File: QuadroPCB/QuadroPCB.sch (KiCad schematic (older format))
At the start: 24 parts, among them IC1 AT24CS02-SSHM, P1 MPU9150, P10 AKKU, P2 stm32discovery_left, P3 stm32discovery_right, P4 rc_signal, P5 Motor3, P6 Motor4, P7 BMP180, P8 Motor1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

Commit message: blubb
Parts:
- added P11: MeisterFluglicht, Pin_Headers:Pin_Header_Straight_1x05, symbol CONN_01X05
- added Q2: Q_NMOS_GSD, Housings_SOT-23_SOT-143_TSOT-6:SOT-23_Handsoldering, symbol Q_NMOS_GSD
- added R6: 1k, Resistors_SMD:R_0805_HandSoldering, symbol R
- added SP2: SPEAKER, Buzzers_Beepers:Buzzer_12x9.5RM7.6, symbol SPEAKER
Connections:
- net +5V: now also SP1.1, SP2.1; no longer SP1.2
- net Beeper_PIN: no longer R4.1
- net GND: now also P11.5 (P5), Q2.2 (S)
- net at Q1.3 (D): now also SP1.2; no longer SP1.1
- net LEDS_SPI_SCK: now reaches P2.35 (P35)
- net LEDS_SPI_SCK: now also P11.1 (P1)
- net LEDS_SPI_SS: now reaches P2.36 (P36)
- net LEDS_SPI_SS: now also P11.2 (P2)
- net LEDS_SPI_MOSI: now reaches P2.37 (P37)
- net LEDS_SPI_MOSI: now also P11.3 (P3)
- net LEDS_SPI_MISO: now reaches P2.38 (P38)
- net LEDS_SPI_MISO: now also P11.4 (P4)
- net Beeper1_PIN: now reaches P3.3 (P3)
- net Beeper1_PIN: now also R6.1
- net Beeper2_PIN: now reaches P3.4 (P4)
- net Beeper2_PIN: now also R4.1
- new net: Q2.1 (G), R6.2
- new net: Q2.3 (D), SP2.2
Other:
- note added: "TODO:\n\nspi pins für leds\nweite pins rausführen?\n"
- note removed: "TODO:\n\nbuzzer pin\nweite pins rausführen?\n"
- moved on the sheet: P1, P4

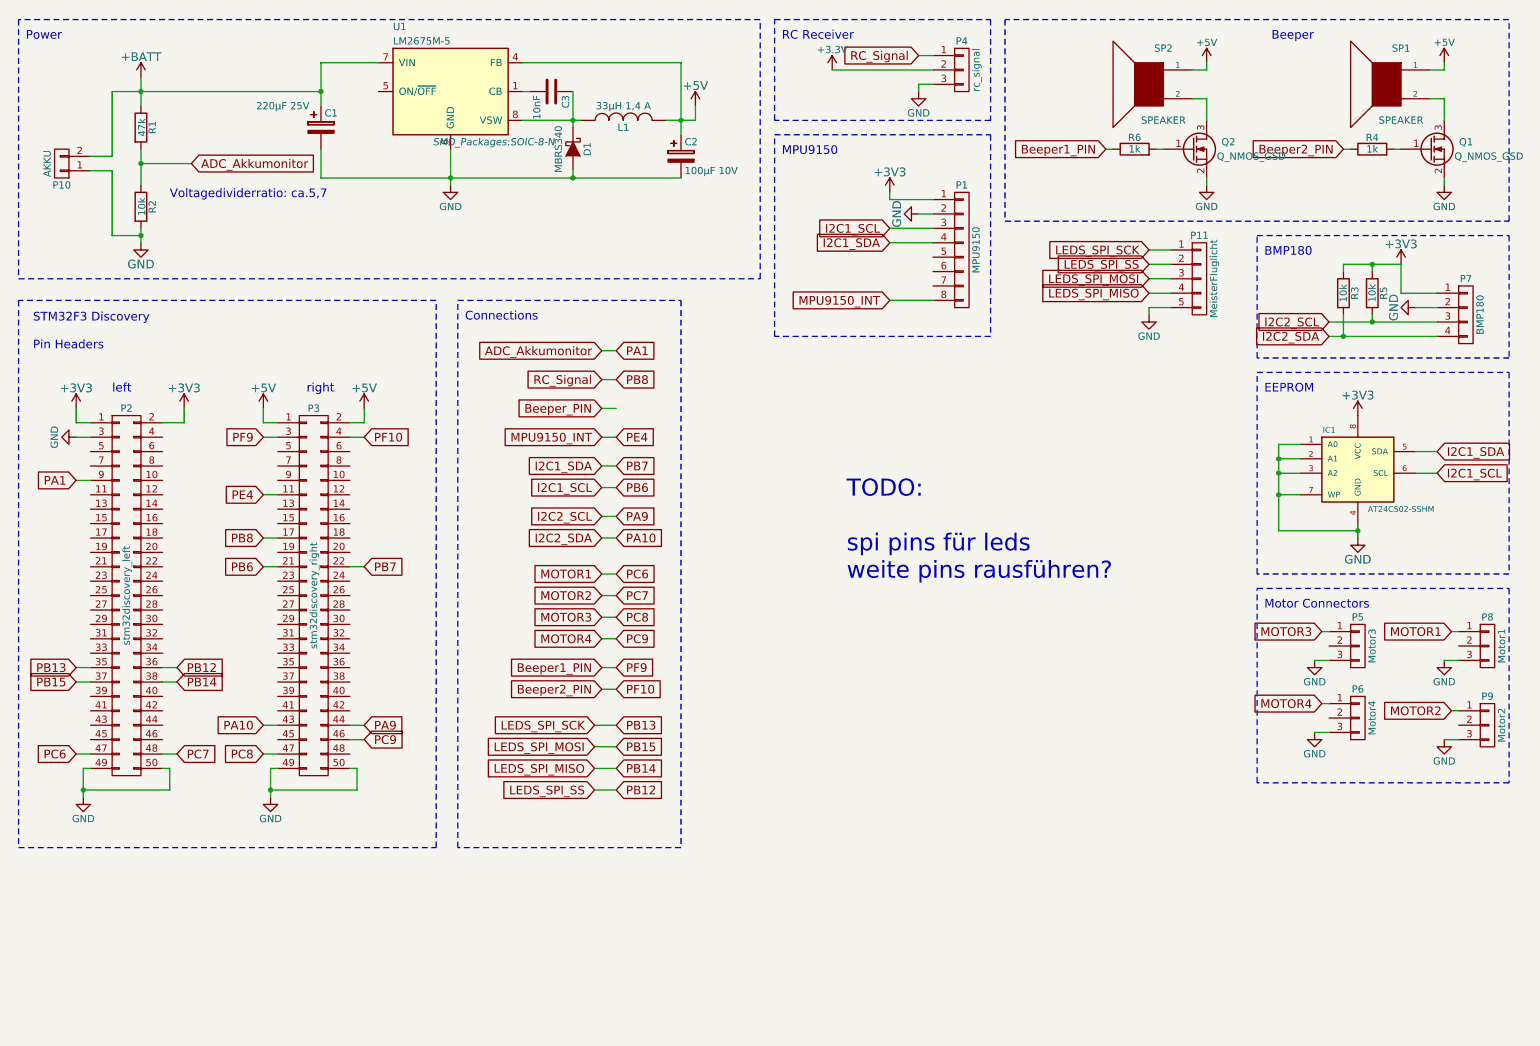
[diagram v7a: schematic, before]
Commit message: step down extern fluglicht auf die platine gepackt
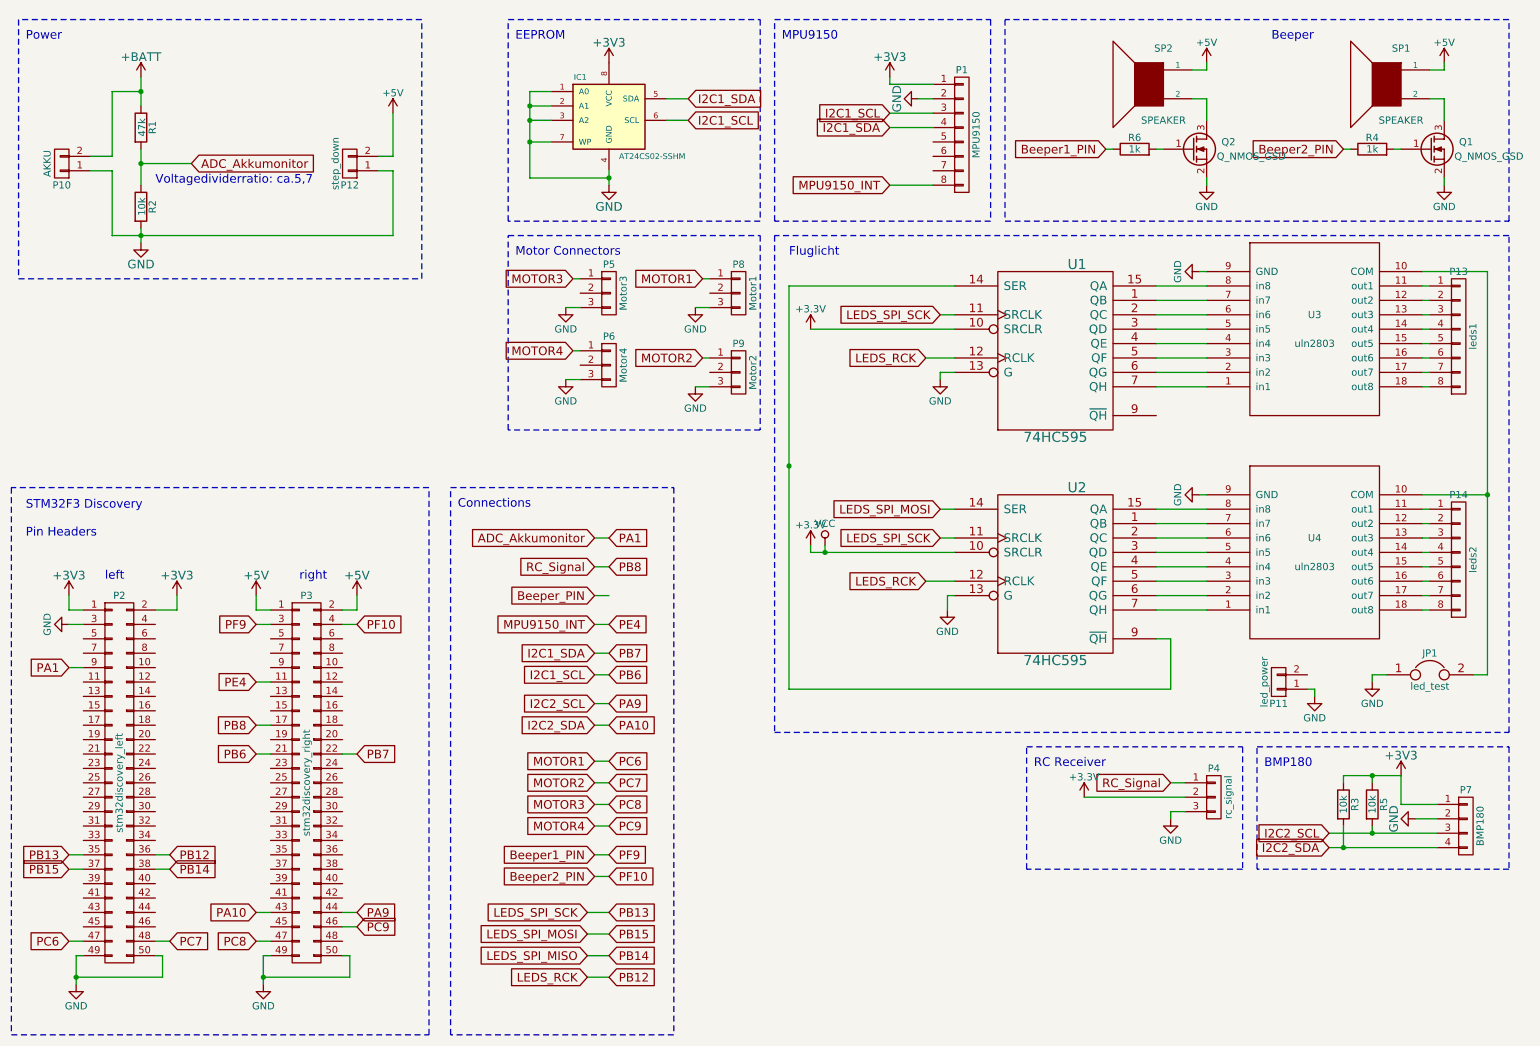
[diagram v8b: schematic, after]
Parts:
- removed C1: 220µF 25V, Capacitors_SMD:c_elec_8x10.5, symbol CP
- removed C2: 100µF 10V, Capacitors_SMD:c_elec_8x6.7, symbol CP
- removed C3: 10nF, Capacitors_SMD:C_0805_HandSoldering, symbol C
- removed D1: MBRS340, Diodes_SMD:Diode-DO-214AB_Handsoldering, symbol D_Schottky
- removed L1: 33µH 1,4 A, Choke_SMD:Choke_SMD_PISN_Handsoldering_FASTRON, symbol INDUCTOR
- removed P11: MeisterFluglicht, Pin_Headers:Pin_Header_Straight_1x05, symbol CONN_01X05
- removed U1: LM2675M-5, SMD_Packages:SOIC-8-N, symbol LM2675M-5
- added JP1: led_test, Pin_Headers:Pin_Header_Straight_1x02, symbol JUMPER
- added P11: led_power, Connect:PINHEAD1-2, symbol CONN_01X02
- added P12: step_down, Connect:PINHEAD1-2, symbol CONN_01X02
- added P13: leds1, Pin_Headers:Pin_Header_Straight_1x08, symbol CONN_01X08
- added P14: leds2, Pin_Headers:Pin_Header_Straight_1x08, symbol CONN_01X08
- added U1, U2: 74HC595, Housings_SOIC:SOIC-16_3.9x9.9mm_Pitch1.27mm, symbol 74HC595
- added U3, U4: uln2803, Housings_SOIC:SOIC-18_7.5x11.6mm_Pitch1.27mm, symbol uln2803
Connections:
- net +3V3: now also U1.10 (SRCLR), U1.16 (VCC), U2.10 (SRCLR), U2.16 (VCC)
- net +5V: now also P12.2 (P2)
- net GND: now also JP1.1, P11.1 (P1), P12.1 (P1), U1.13 (G), U1.8 (GND), U2.13 (G), U2.8 (GND), U3.9 (GND), U4.9 (GND)
- net LEDS_SPI_MOSI: now also U2.14 (SER)
- net LEDS_SPI_SCK: now also U1.11 (SRCLK), U2.11 (SRCLK)
- net LEDS_SPI_SS renamed LEDS_RCK
- net LEDS_RCK: now also U1.12 (RCLK), U2.12 (RCLK)
- new net: U2.1 (QB), U4.7 (in7)
- new net: U2.15 (QA), U4.8 (in8)
- new net: U2.2 (QC), U4.6 (in6)
- new net: U2.3 (QD), U4.5 (in5)
- new net: U2.4 (QE), U4.4 (in4)
- new net: U2.5 (QF), U4.3 (in3)
- new net: U2.6 (QG), U4.2 (in2)
- new net: U2.7 (QH), U4.1 (in1)
- new net: U1.14 (SER), U2.9 (~QH)
- new net: JP1.2, U3.10 (COM), U4.10 (COM)
- new net: P14.1 (P1), U4.11 (out1)
- new net: P14.2 (P2), U4.12 (out2)
- new net: P14.3 (P3), U4.13 (out3)
- new net: P14.4 (P4), U4.14 (out4)
- new net: P14.5 (P5), U4.15 (out5)
- new net: P14.6 (P6), U4.16 (out6)
- new net: P14.7 (P7), U4.17 (out7)
- new net: P14.8 (P8), U4.18 (out8)
- new net: U1.1 (QB), U3.7 (in7)
- new net: U1.15 (QA), U3.8 (in8)
- new net: U1.2 (QC), U3.6 (in6)
- new net: U1.3 (QD), U3.5 (in5)
- new net: U1.4 (QE), U3.4 (in4)
- new net: U1.5 (QF), U3.3 (in3)
- new net: U1.6 (QG), U3.2 (in2)
- new net: U1.7 (QH), U3.1 (in1)
- new net: P13.1 (P1), U3.11 (out1)
- new net: P13.2 (P2), U3.12 (out2)
- new net: P13.3 (P3), U3.13 (out3)
- new net: P13.4 (P4), U3.14 (out4)
- new net: P13.5 (P5), U3.15 (out5)
- new net: P13.6 (P6), U3.16 (out6)
- new net: P13.7 (P7), U3.17 (out7)
- new net: P13.8 (P8), U3.18 (out8)
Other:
- note added: "Fluglicht"
- note removed: "TODO:\n\nspi pins für leds\nweite pins rausführen?\n"
- moved on the sheet: IC1, P1, P2, P3, P4, P5, P6, P7, P8, P9, R3, R5
